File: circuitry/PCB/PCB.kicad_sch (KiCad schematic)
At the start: 14 parts

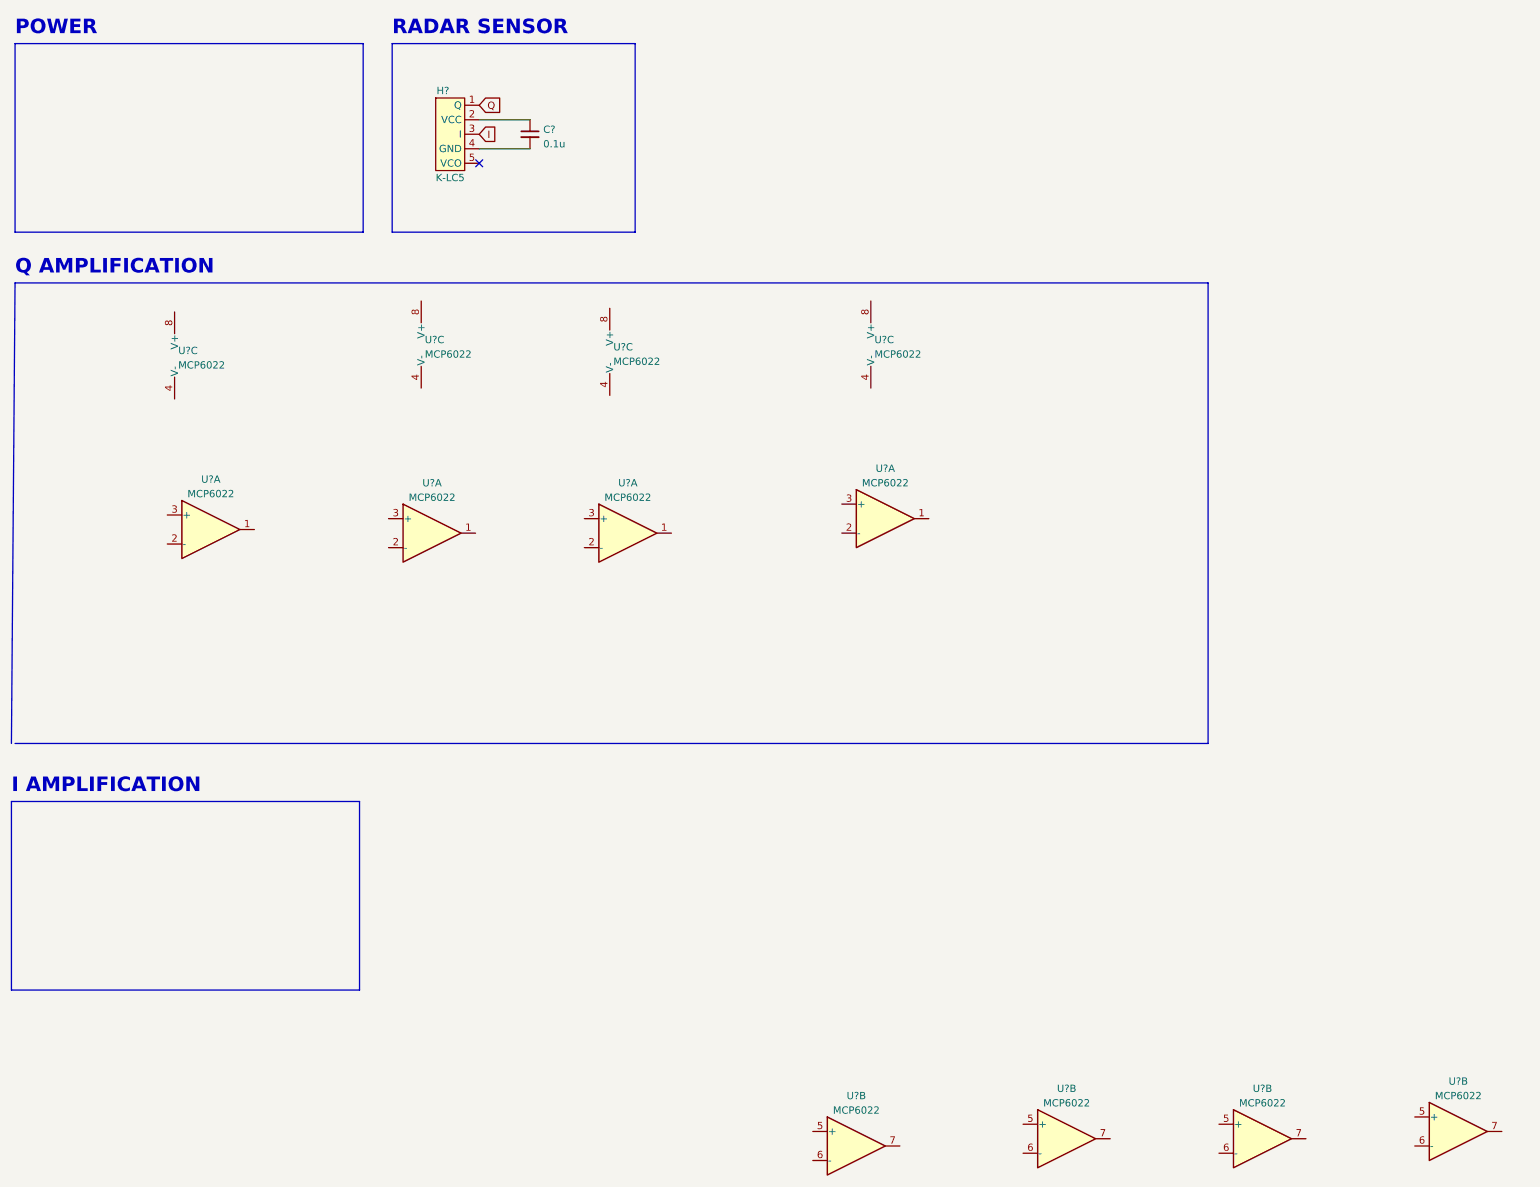
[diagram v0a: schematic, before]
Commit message: schematic update
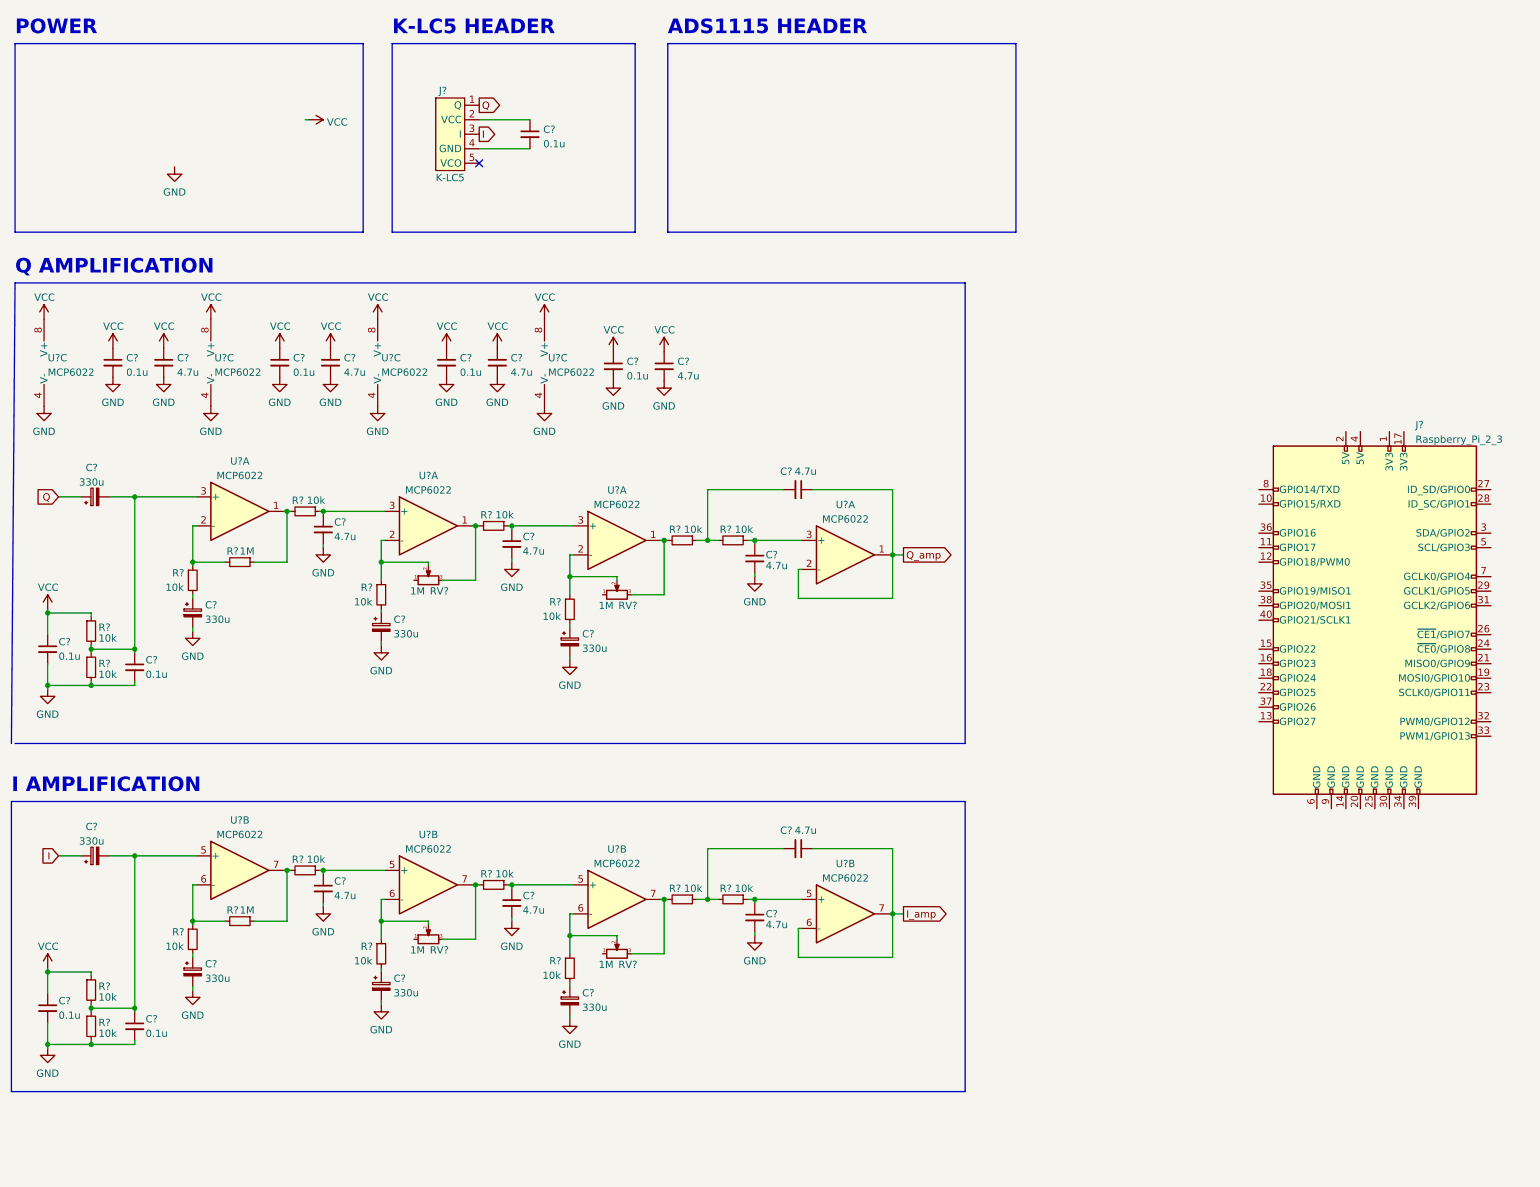
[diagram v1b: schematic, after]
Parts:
- added C? (x8): 0.1u, symbol Device:C_Small
- added C? (x8): 330u, symbol Device:C_Polarized_Small
- added C? (x12): 4.7u, symbol Device:C_Small
- added J?: Raspberry_Pi_2_3, symbol Connector:Raspberry_Pi_2_3
- added R? (x18): 10k, symbol Device:R_Small
- added R? (x2): 1M, symbol Device:R_Small
- added RV? (x4): 1M, symbol Device:R_Potentiometer_Small
- gave numbers to parts that had none: 1
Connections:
- net I: now also C?.1
- net Q: now also C?.1
- net at U?.5 (+): now also C?.1, R?.1 (x3)
- net at U?.6 (-): now also R?.1, RV?.2 (x2)
- net at U?.7: now also R?.2, RV?.3 (x2)
- net GND: now reaches U?.4 (V-)
- net GND: now also U?.4 (V-), U?.4 (V-), U?.4 (V-), C?.2, C?.2, C?.2, C?.2, C?.2, C?.2, C?.2, C?.2, C?.2, C?.2, C?.2, C?.2, C?.2, C?.2, C?.2, C?.2, C?.2, C?.2, C?.2, C?.2, C?.2, C?.2, C?.2, C?.2, R?.2, R?.2
- net VCC: now reaches U?.8 (V+)
- net VCC: now also U?.8 (V+), U?.8 (V+), U?.8 (V+), C?.1, C?.1, C?.1, C?.1, C?.1, C?.1, C?.1, C?.1, C?.1, C?.1, R?.1, R?.1
- net at U?.1: now also R?.2, RV?.3 (x2)
- net at U?.2 (-): now also R?.1, RV?.2 (x2)
- net at U?.3 (+): now also C?.1, R?.1 (x3)
- net at U?.1: now also R?.1, R?.2
- net at U?.2 (-): now also R?.1, R?.2
- net at U?.3 (+): now also C?.1, C?.2, R?.1, R?.2
- net at U?.5 (+): now also C?.1, C?.2, R?.1, R?.2
- net at U?.6 (-): now also R?.1, R?.2
- net at U?.7: now also R?.1, R?.2
- net Q_amp: now reaches U?.1
- net Q_amp: now also U?.2 (-), C?.1
- net I_amp: now reaches U?.6 (-)
- net I_amp: now also U?.7, C?.1
- new net: C?.1, R?.2 (x6)
- new net: C?.2, R?.1, R?.2 (x2)
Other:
- note added: "ADS1115 HEADER"
- note added: "K-LC5 HEADER"
- note removed: "RADAR SENSOR"
- moved on the sheet: U?A, U?B, U?C

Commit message: finish temporary schematic
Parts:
- added C12, C3: 4.7u, symbol Device:C_Small
- added J2: ADS1115, symbol Proj_Lib:ADS1115
- added J3: I/Q-amp, symbol Proj_Lib:I/Q-amp
- added SW1: SW_SPDT, symbol Switch:SW_SPDT
- added U2: AP2138N-3.3TRG1, symbol Proj_Lib:AP2138N-3.3TRG1
- gave numbers to parts that had none: 59
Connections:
- net GND: now also C23.2, J1.4 (GND), J4.6 (GND), C12.2, C3.2, J2.2 (GND), J2.5 (ADDR), SW1.1 (A), U2.2 (GND)
- net I: now also C5.2; no longer C5.1
- net I_amp: now also J2.8 (A1), J3.2 (I_amp)
- net Q: now also C4.2; no longer C4.1
- net Q_amp: now also J2.7 (A0), J3.1 (Q_amp)
- net VCC: now also C23.1, J1.2 (VCC), C12.1, J2.1 (VDD), U2.5 (Vout)
- net at C8.1, R3.2, R4.1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: now also C5.1; no longer C5.2
- net at C7.1, R1.2, R2.1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: now also C4.1; no longer C4.2
- net 5V: now reaches J4.2 (5V)
- net 5V: now also C3.1, SW1.3 (C), U2.1 (Vin)
- net SDA: now reaches J4.3 (SDA/GPIO2)
- net SDA: now also J2.4 (SDA)
- net SCL: now reaches J4.5 (SCL/GPIO3)
- net SCL: now also J2.3 (SCL)
- new net: SW1.2 (B), U2.3 (CE)
- no-connect marks 1 -> 44
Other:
- note added: "I/Q OUTPUT HEADER"
- note added: "RPI HEADER"
- moved on the sheet: C1, C10, C11, C13, C14, C15, C16, C17, C18, C19, C2, C20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

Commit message: initial board layout
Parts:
- C1, C12, C13, C14, C15, C16, C19, C2, C20, C21, C22, C23, C26, C27, C28, C29, C3, C30, C31, C6, C7, C8, C9, R1, R10, R11, R12, R13, R14, R15, R16, R17, R18, R19, R2, R20, R3, R4, R5, R6, R7, R8, R9: footprint (none) -> Capacitor_SMD:C_1206_3216Metric_Pad1.33x1.80mm_HandSolder
- C10, C11, C17, C18, C24, C25, C4, C5: footprint (none) -> Capacitor_THT:CP_Radial_D8.0mm_P2.50mm
- J1: footprint (none) -> Connector_PinSocket_2.54mm:PinSocket_1x05_P2.54mm_Vertical
- J2: footprint (none) -> Connector_PinSocket_2.54mm:PinSocket_1x10_P2.54mm_Vertical
- J3: footprint (none) -> Connector_PinSocket_2.54mm:PinSocket_1x02_P2.54mm_Vertical
- J4: footprint (none) -> Connector_PinSocket_2.54mm:PinSocket_2x20_P2.54mm_Vertical

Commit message: layout update
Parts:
- R1, R10, R11, R12, R13, R14, R15, R16, R17, R18, R19, R2, R20, R3, R4, R5, R6, R7, R8, R9: footprint Capacitor_SMD:C_1206_3216Metric_Pad1.33x1.80mm_HandSolder -> Resistor_SMD:R_1206_3216Metric_Pad1.30x1.75mm_HandSolder
